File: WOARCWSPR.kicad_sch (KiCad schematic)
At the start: 22 parts, among them J1 Raspberry_Pi_2_3, J2 TP1, J3 TP2, J4 TP2, J5 Conn_Coaxial, J6 TP2, Q1 BS170, SW1 SW_Push_Dual

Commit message: V1.0
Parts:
- removed LPF1: ~, symbol QRPLabs:LPF
- added C4: 100n, Capacitor_THT:CP_Radial_D5.0mm_P2.50mm, symbol Device:C
- added J5: LPF_OUT, Connector_PinHeader_2.54mm:PinHeader_1x04_P2.54mm_Vertical, symbol Connector:Conn_01x04_Pin
- added J6: LPF_IN, Connector_PinHeader_2.54mm:PinHeader_1x04_P2.54mm_Vertical, symbol Connector:Conn_01x04_Pin
- C1: renamed from C3; footprint (none) -> Capacitor_THT:CP_Radial_D5.0mm_P2.50mm; symbol Device:C -> Device:C_Polarized
- C2, C3: renamed from C1; footprint (none) -> Capacitor_THT:CP_Radial_D5.0mm_P2.50mm
- D1: footprint (none) -> LED_SMD:LED_1210_3225Metric_Pad1.42x2.65mm_HandSolder
- J1: renamed from J4; footprint (none) -> Connector_PinHeader_2.54mm:PinHeader_1x01_P2.54mm_Vertical
- J3: renamed from J6; footprint (none) -> Connector_PinHeader_2.54mm:PinHeader_1x01_P2.54mm_Vertical
- J4: renamed from J5; footprint (none) -> Connector_Coaxial:SMA_Samtec_SMA-J-P-H-ST-EM1_EdgeMount
- J7: renamed from J2; footprint (none) -> Connector_PinHeader_2.54mm:PinHeader_1x01_P2.54mm_Vertical
- J8: renamed from J3; footprint (none) -> Connector_PinHeader_2.54mm:PinHeader_1x01_P2.54mm_Vertical
- L1: footprint (none) -> Inductor_THT:L_Axial_L9.5mm_D4.0mm_P15.24mm_Horizontal_Fastron_SMCC
- R2, R3, R4, R5, R6, R7: footprint (none) -> Resistor_THT:R_Axial_DIN0207_L6.3mm_D2.5mm_P7.62mm_Horizontal
- RV1: footprint (none) -> Potentiometer_THT:Potentiometer_Piher_PT-6-V_Vertical
- SW1: footprint (none) -> Button_Switch_THT:SW_PUSH_6mm
- renumbered J1 to J2
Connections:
- net GND: now also J2.14 (GND), J2.20 (GND), J2.25 (GND), J2.30 (GND), J2.34 (GND), J2.39 (GND), J2.6 (GND), J2.9 (GND), C4.1, J5.3 (Pin_3), J5.4 (Pin_4), J6.1 (Pin_1), J6.2 (Pin_2); no longer J3.1 (Pin_1), R7.1
- net at C3.2: now also J6.3 (Pin_3), J6.4 (Pin_4)
- net at D2.2 (A), J4.1 (In): now also J5.1 (Pin_1), J5.2 (Pin_2)
- new net: C4.2, J3.1 (Pin_1), R7.1
- no-connect marks 6 -> 2

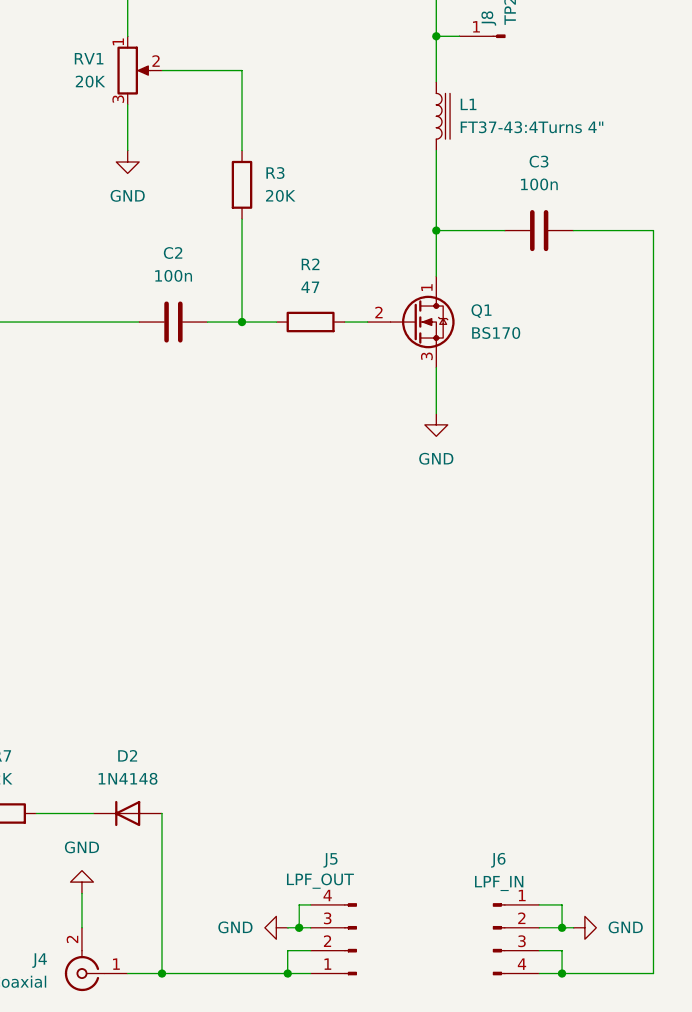
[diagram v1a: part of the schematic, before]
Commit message: Correct pin layout for filter board
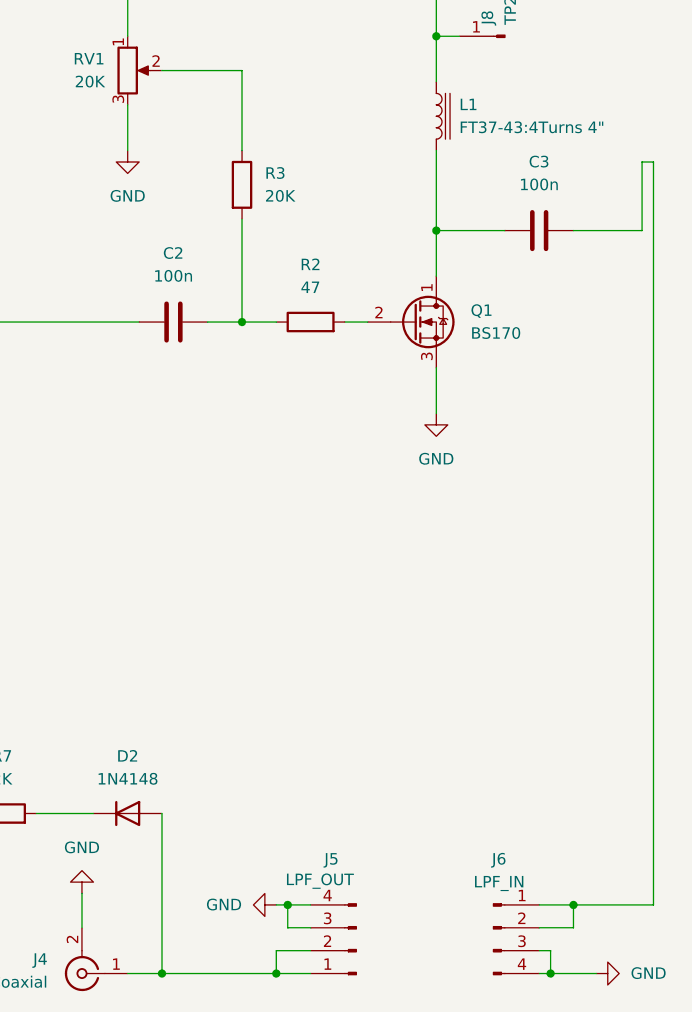
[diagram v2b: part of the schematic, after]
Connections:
- net GND: now also J6.3 (Pin_3), J6.4 (Pin_4); no longer J6.1 (Pin_1), J6.2 (Pin_2)
- new net: C3.2, J6.1 (Pin_1), J6.2 (Pin_2)

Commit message: Change to ceramic cap footprints
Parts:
- C2, C3, C4: footprint Capacitor_THT:CP_Radial_D5.0mm_P2.50mm -> Capacitor_THT:C_Disc_D6.0mm_W2.5mm_P5.00mm
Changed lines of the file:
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@@
 			)
 		)
-		(property "Footprint" "Capacitor_THT:CP_Radial_D5.0mm_P2.50mm"
+		(property "Footprint" "Capacitor_THT:C_Disc_D6.0mm_W2.5mm_P5.00mm"
 			(at 234.95 67.6148 0)
 			(effects
@@
 			)
 		)
-		(property "Footprint" "Capacitor_THT:CP_Radial_D5.0mm_P2.50mm"
+		(property "Footprint" "Capacitor_THT:C_Disc_D6.0mm_W2.5mm_P5.00mm"
 			(at 154.94 132.3848 0)
 			(effects
@@
 			)
 		)
-		(property "Footprint" "Capacitor_THT:CP_Radial_D5.0mm_P2.50mm"
+		(property "Footprint" "Capacitor_THT:C_Disc_D6.0mm_W2.5mm_P5.00mm"
 			(at 194.31 77.7748 0)
 			(effects

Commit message: Swap to 3mm THT LED
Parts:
- D1: footprint LED_SMD:LED_1210_3225Metric_Pad1.42x2.65mm_HandSolder -> LED_THT:LED_D3.0mm
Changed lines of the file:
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@@
 			)
 		)
-		(property "Footprint" "LED_SMD:LED_1210_3225Metric_Pad1.42x2.65mm_HandSolder"
+		(property "Footprint" "LED_THT:LED_D3.0mm"
 			(at 104.14 76.2 0)
 			(effects

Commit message: Update SMA footprint for correct size of connector
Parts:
- J4: footprint Connector_Coaxial:SMA_Samtec_SMA-J-P-H-ST-EM1_EdgeMount -> Connector_Coaxial:SMA_Amphenol_132289_EdgeMount
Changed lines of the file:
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@@
 			)
 		)
-		(property "Footprint" "Connector_Coaxial:SMA_Samtec_SMA-J-P-H-ST-EM1_EdgeMount"
+		(property "Footprint" "Connector_Coaxial:SMA_Amphenol_132289_EdgeMount"
 			(at 180.34 151.13 0)
 			(effects
